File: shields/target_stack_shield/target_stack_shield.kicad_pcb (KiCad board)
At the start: 4 copper layers, 85 x 56 mm, 43 parts, among them IC1 NCP1117DT33T5G, J1 GPIO shield connector 40pin, J2 probe shield connector 26pin, J3 PCIE-064-02-X-D-RA, U1 SN74CB3T16211DGGR, U2 SN74CB3T16211DGGR, U3 SN74CB3T16211DGGR, U4 SN74CB3T16211DGGR, U5 PCA9535CPW,118

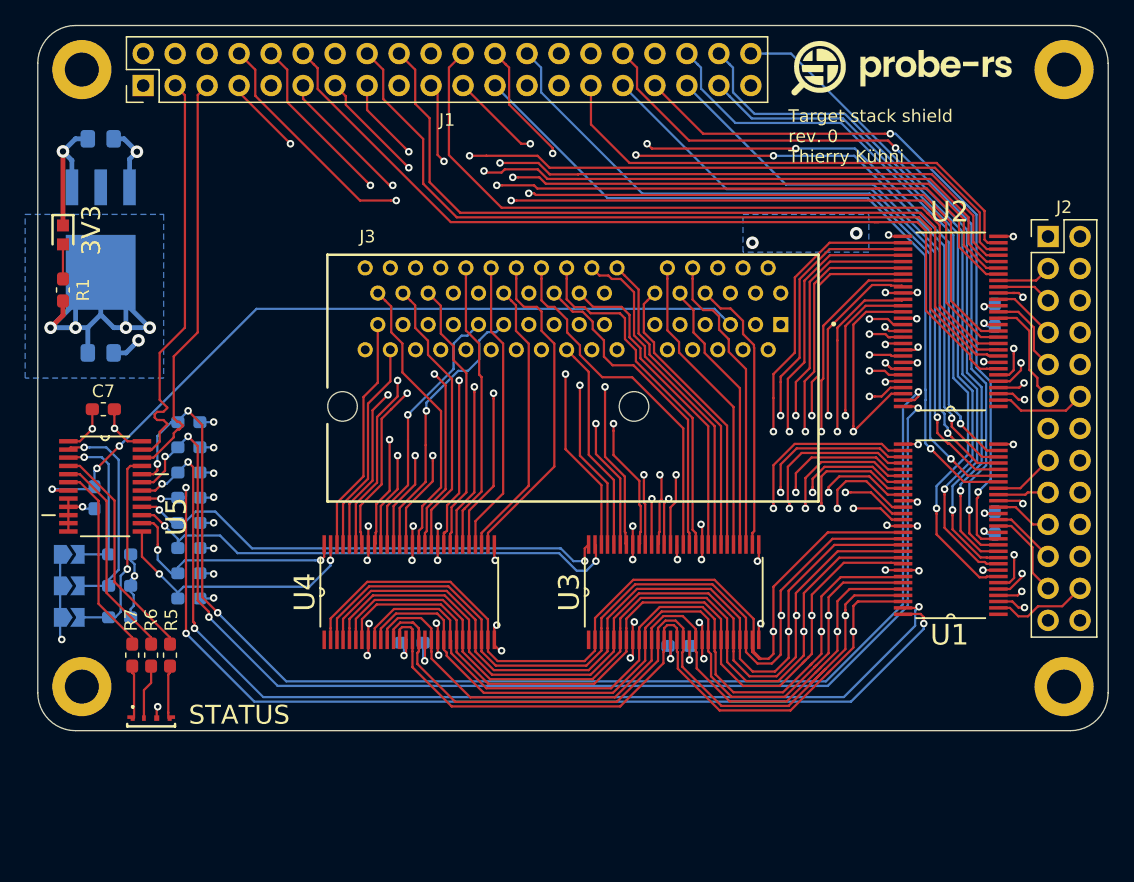
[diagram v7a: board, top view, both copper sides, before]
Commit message: changed PCIE 64 to M.2 Key B connector
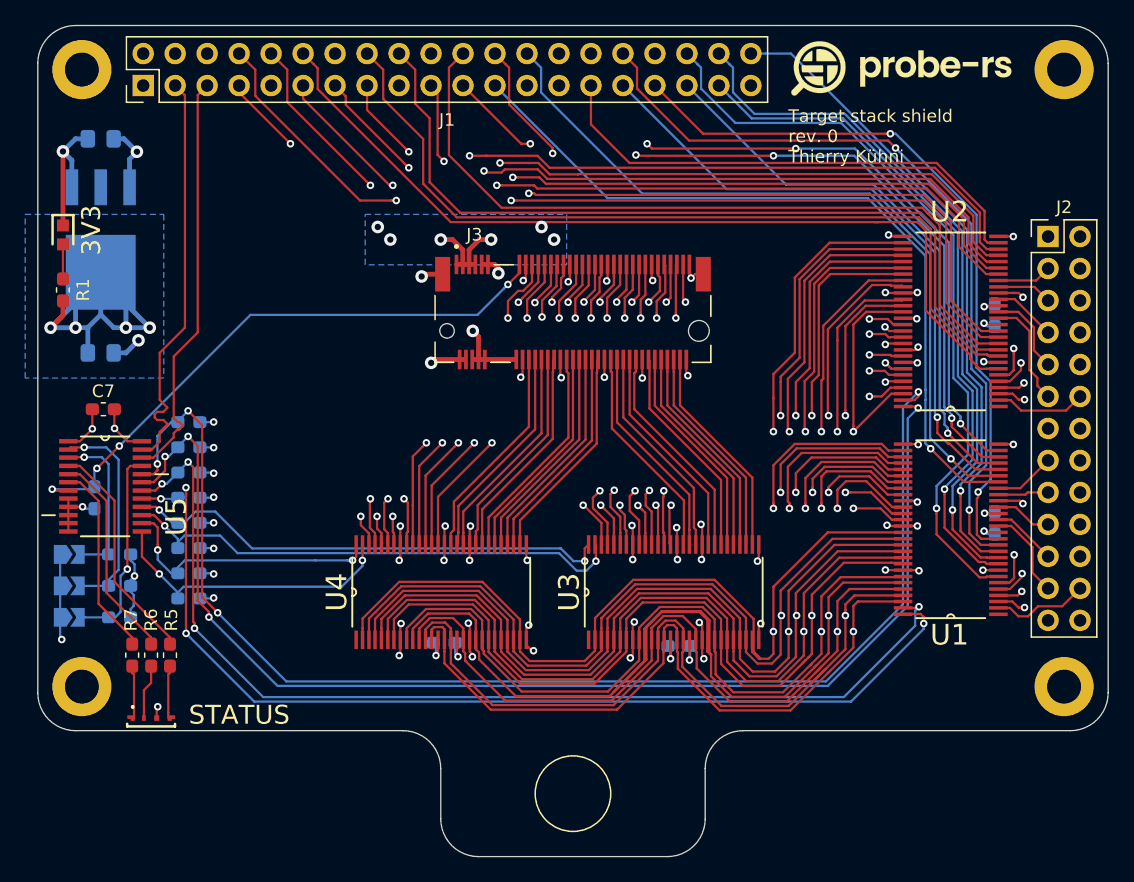
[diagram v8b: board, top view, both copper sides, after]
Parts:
- J3: value PCIE-064-02-X-D-RA -> m2_keyA_67pin; footprint hive:SAMTEC_PCIE-064-02-X-D-RA -> hive:TE_2199230-3
- moved REF** 12.4 mm to (148.4, 84.6)
- moved J3 3.75 mm to (152.5, 78.2)
- moved C6 2.54 mm to (142.3, 103.0)
- moved U4 2.54 mm to (142.0, 99.0)
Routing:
- net /Bus switches/BUS_TCK|SWDCLK: track 109.9 -> 137.4 mm
- net GND: track 92.5 -> 115.1 mm, vias 50 -> 64
- net /BOARD_DETECT: track 62.4 -> 47.0 mm, vias 3 -> 4
- net /TGT_UART_TxD2: track 17.0 -> 28.5 mm, vias 0 -> 2
- net /TGT_GPIO2.2: track 17.4 -> 28.9 mm, vias 1 -> 2
- net /TGT_RST_1: track 28.3 -> 17.1 mm
- net /TGT_GPIO2.0: track 17.6 -> 28.7 mm, vias 1 -> 2
- net /TGT_TDO|SWO_1: track 28.0 -> 17.1 mm
- net /TGT_TMS|SWDIO_2: track 18.3 -> 28.7 mm, vias 1 -> 2
- net /TGT_UART_RxD2: track 18.8 -> 28.7 mm, vias 0 -> 2
- net /TGT_GPIO2.3: track 19.2 -> 28.8 mm, vias 1 -> 2
- net /TGT_TDI|NC_3: track 26.8 -> 17.3 mm, vias 1 -> 0
- net /TGT_TMS|SWDIO_1: track 26.8 -> 17.4 mm
- net /TGT_TDO|SWO_2: track 18.7 -> 28.0 mm, vias 1 -> 2
- net /TGT_GPIO2.1: track 19.7 -> 28.8 mm, vias 1 -> 2
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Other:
- board size 85 x 56 mm -> 85 x 66 mm
